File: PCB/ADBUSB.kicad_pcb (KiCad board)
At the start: 2 copper layers, 39.3 x 36.6 mm, 7 parts, among them J1 MLD-MDC-4-02, J2 MLD-MDC-4-02, SW1 SW_SPST, U1 ProMicro

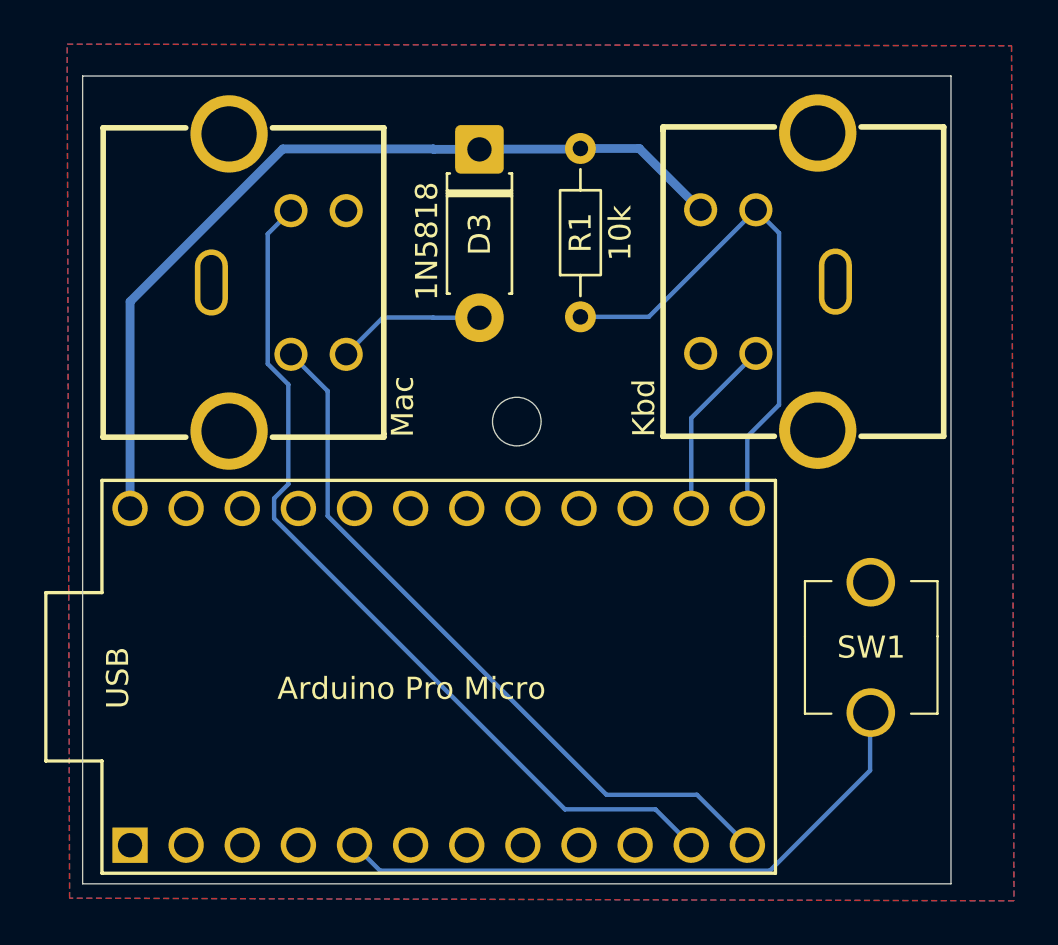
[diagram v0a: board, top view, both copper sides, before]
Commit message: Add a second button footprint
So one can either use an horizontal or vertical one
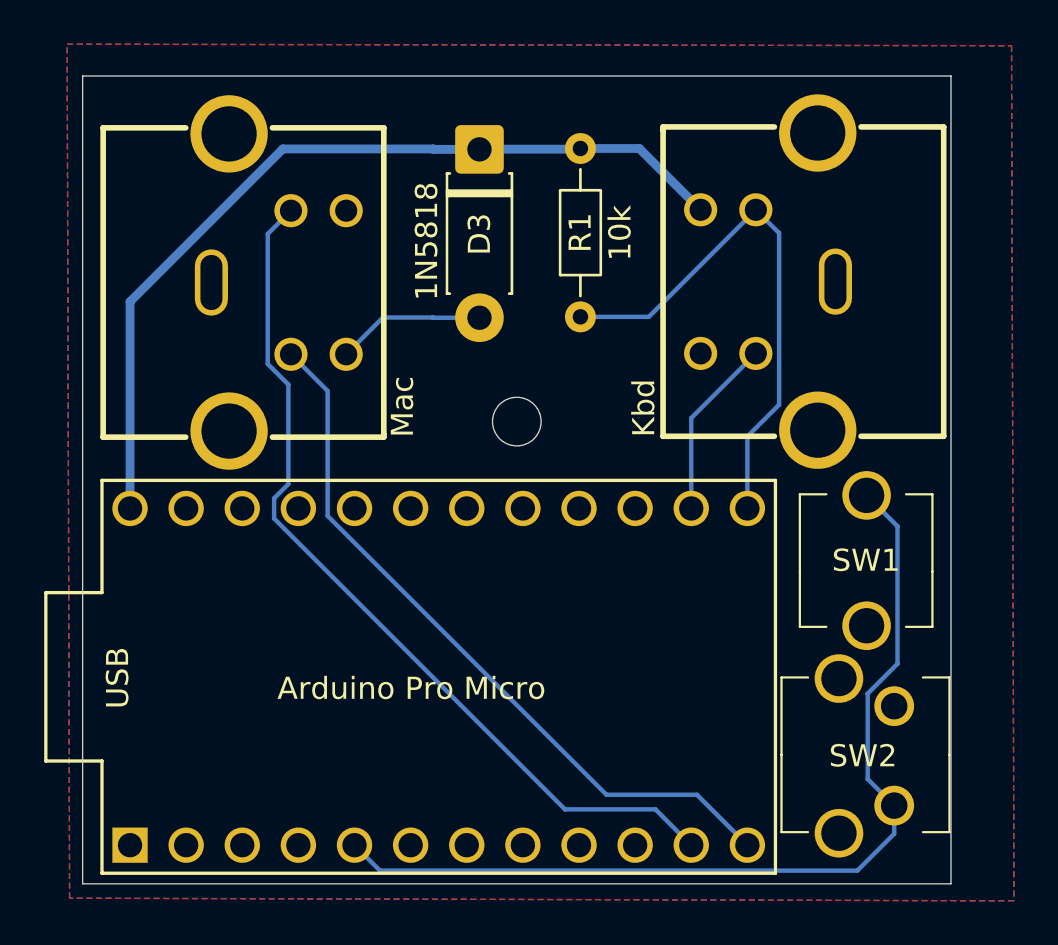
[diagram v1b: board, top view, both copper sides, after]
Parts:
- added SW2: SW_SPST, Pushbutton:SPST_power_switch, F.Cu at (171.8, 91.2)
- moved SW1 3.14 mm to (172.6, 82.9), turned to 90 degrees
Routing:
- net Net-(U1-SDA): track 28.3 -> 42.5 mm
